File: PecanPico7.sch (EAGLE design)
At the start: 178 parts, among them IC1 Si4060-B1B-FM, IC10 TPS62260DRVT, IC11 TPS62261DRVT, IC12 TPS63021, IC13 RF6886, IC14 TPS78227DDCR, IC16 PAC1720-1-AIA-TR, IC2 Si4060-B1B-FM, IC3 BME280_BME280, IC4 uBlox MAX7/8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

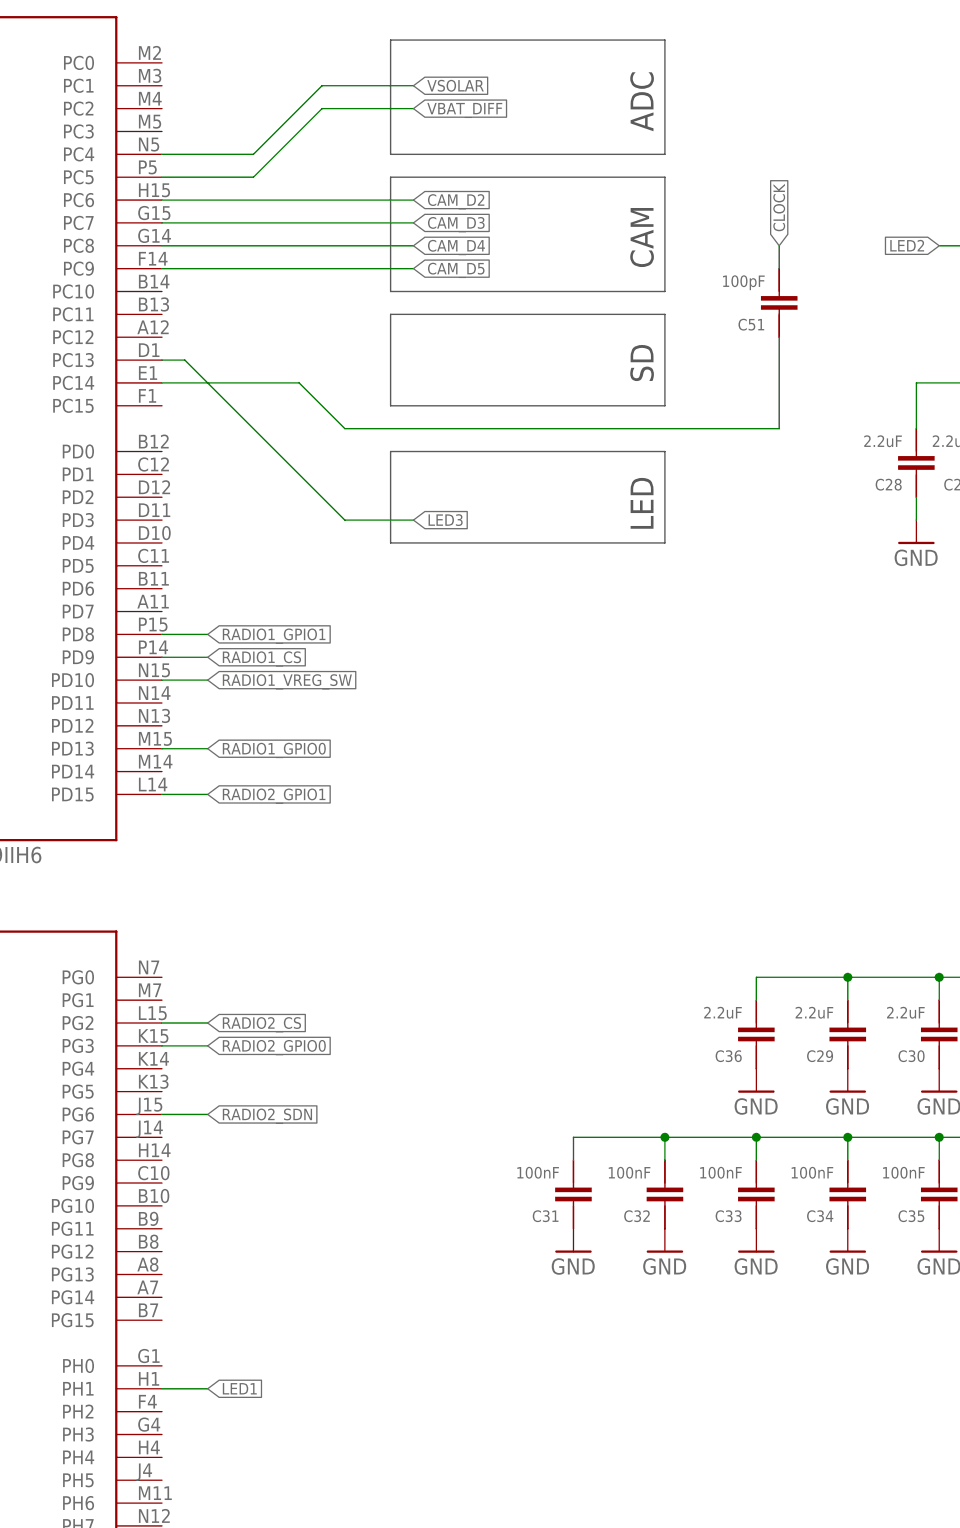
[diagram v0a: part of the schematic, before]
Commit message: Connected TCXO to STM32_OSC pin
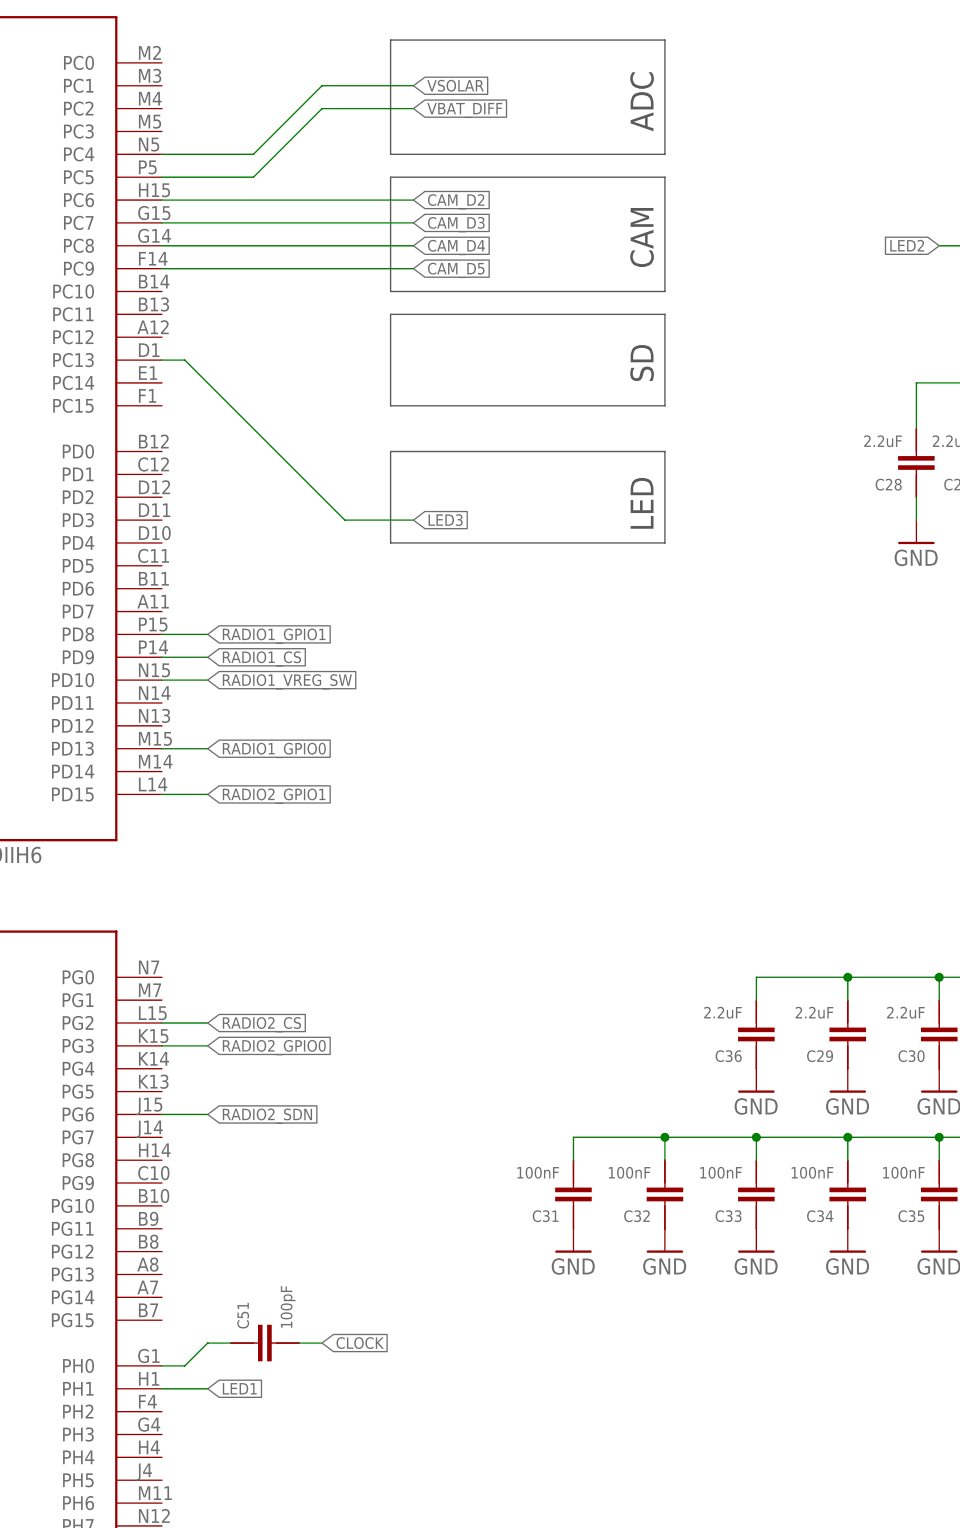
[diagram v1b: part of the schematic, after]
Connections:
- net N$39: now also IC5G$2.PH0; no longer IC5G$1.PC14
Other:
- moved on the sheet: C51
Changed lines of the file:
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@@
 <instance part="L14" gate="G$1" x="-22.86" y="447.04" rot="R180"/>
 <instance part="P+17" gate="G$1" x="10.16" y="447.04" rot="R270"/>
-<instance part="C51" gate="G$1" x="-76.2" y="195.58" rot="R180"/>
+<instance part="C51" gate="G$1" x="-134.62" y="81.28" rot="R90"/>
 <instance part="IC16" gate="A" x="-180.34" y="462.28"/>
 <instance part="P+23" gate="G$1" x="-200.66" y="482.6"/>
@@
 <segment>
 <pinref part="C51" gate="G$1" pin="1"/>
-<wire x1="-76.2" y1="200.66" x2="-76.2" y2="203.2" width="0.1524" layer="91"/>
-<label x="-76.2" y="203.2" size="1.27" layer="95" rot="R90" xref="yes"/>
+<wire x1="-129.54" y1="81.28" x2="-127" y2="81.28" width="0.1524" layer="91"/>
+<label x="-127" y="81.28" size="1.27" layer="95" xref="yes"/>
 </segment>
 <segment>
@@
 <net name="N$39" class="0">
 <segment>
-<pinref part="IC5" gate="G$1" pin="PC14"/>
-<wire x1="-144.78" y1="187.96" x2="-129.54" y2="187.96" width="0.1524" layer="91"/>
-<wire x1="-129.54" y1="187.96" x2="-124.46" y2="182.88" width="0.1524" layer="91"/>
-<wire x1="-124.46" y1="182.88" x2="-76.2" y2="182.88" width="0.1524" layer="91"/>
-<wire x1="-76.2" y1="182.88" x2="-76.2" y2="193.04" width="0.1524" layer="91"/>
 <pinref part="C51" gate="G$1" pin="2"/>
-</segment>
-</net>
+<wire x1="-137.16" y1="81.28" x2="-139.7" y2="81.28" width="0.1524" layer="91"/>
+<wire x1="-139.7" y1="81.28" x2="-142.24" y2="78.74" width="0.1524" layer="91"/>
+<wire x1="-142.24" y1="78.74" x2="-144.78" y2="78.74" width="0.1524" layer="91"/>
+<pinref part="IC5" gate="G$2" pin="PH0"/>
+</segment>
+</net>

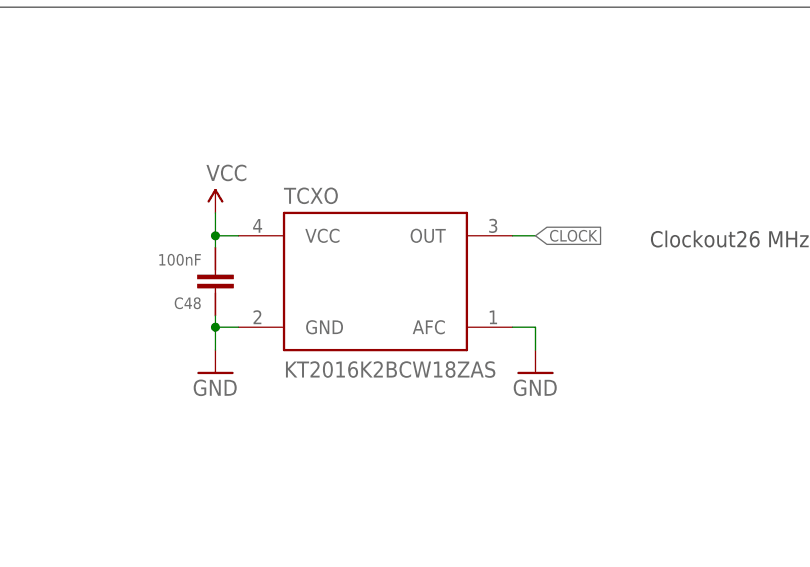
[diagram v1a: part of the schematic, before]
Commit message: Replaced small TCXO package to larger one
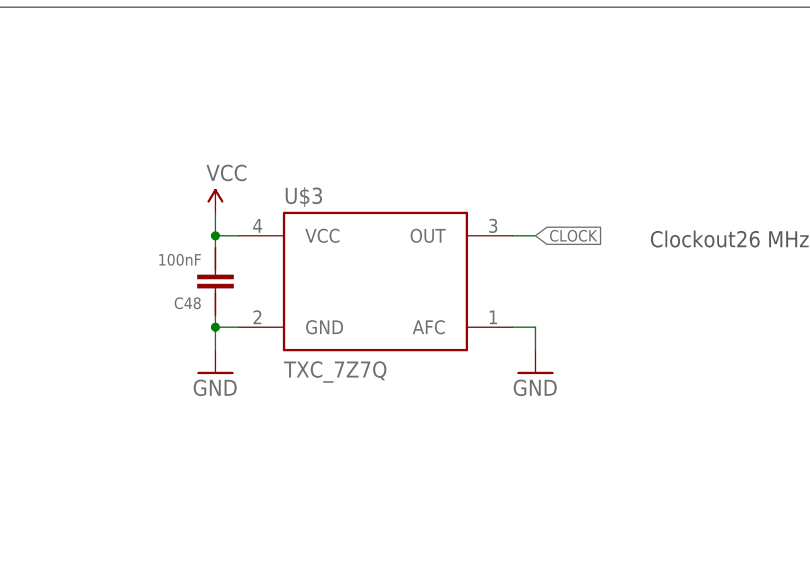
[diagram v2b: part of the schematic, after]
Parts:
- removed TCXO: KT2016K2BCW18ZAS, PecanFemto3:TXC_7Z
- added U$3: TXC_7Z7Q, PecanFemto3:TXC_7Z7Q
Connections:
- net CLOCK: now also U$3.OUT; no longer TCXO.OUT
- net GND: now also U$3.AFC, U$3.GND; no longer TCXO.AFC, TCXO.GND
- net VCC: now also U$3.VCC; no longer TCXO.VCC
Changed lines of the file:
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@@
 <?xml version="1.0" encoding="utf-8"?>
 <!DOCTYPE eagle SYSTEM "eagle.dtd">
-<eagle version="7.3.0">
+<eagle version="7.2.0">
 <drawing>
 <settings>
@@
 <part name="C47" library="PecanFemto3" deviceset="CAP-0805" device="" value="10uF"/>
 <part name="GND61" library="PecanPico6" deviceset="GND" device=""/>
-<part name="TCXO" library="PecanFemto3" deviceset="TXC_7Z" device="" value="KT2016K2BCW18ZAS"/>
 <part name="GND62" library="PecanPico6" deviceset="GND" device=""/>
 <part name="P+21" library="PecanPico6" deviceset="3.3V" device="" value="VCC"/>
@@
 <part name="GND122" library="PecanPico6" deviceset="GND" device=""/>
 <part name="GND123" library="PecanPico6" deviceset="GND" device=""/>
+<part name="U$3" library="PecanFemto3" deviceset="TXC_7Z" device="7Q"/>
 </parts>
 <sheets>
@@
 <instance part="C47" gate="G$1" x="-147.32" y="391.16"/>
 <instance part="GND61" gate="1" x="-147.32" y="373.38"/>
-<instance part="TCXO" gate="TCXO" x="175.26" y="60.96"/>
 <instance part="GND62" gate="1" x="157.48" y="50.8"/>
 <instance part="P+21" gate="G$1" x="157.48" y="68.58"/>
@@
 <instance part="GND122" gate="1" x="-17.78" y="469.9"/>
 <instance part="GND123" gate="1" x="-66.04" y="469.9"/>
+<instance part="U$3" gate="TCXO" x="175.26" y="60.96"/>
 </instances>
 <busses>
@@
 <pinref part="GND62" gate="1" pin="GND"/>
 <wire x1="157.48" y1="53.34" x2="157.48" y2="55.88" width="0.1524" layer="91"/>
-<pinref part="TCXO" gate="TCXO" pin="GND"/>
 <wire x1="157.48" y1="55.88" x2="160.02" y2="55.88" width="0.1524" layer="91"/>
 <pinref part="C48" gate="G$1" pin="2"/>
 <wire x1="157.48" y1="55.88" x2="157.48" y2="57.15" width="0.1524" layer="91"/>
 <junction x="157.48" y="55.88"/>
-</segment>
-<segment>
-<pinref part="TCXO" gate="TCXO" pin="AFC"/>
+<pinref part="U$3" gate="TCXO" pin="GND"/>
+</segment>
+<segment>
 <wire x1="190.5" y1="55.88" x2="193.04" y2="55.88" width="0.1524" layer="91"/>
 <wire x1="193.04" y1="55.88" x2="193.04" y2="53.34" width="0.1524" layer="91"/>
 <pinref part="GND63" gate="1" pin="GND"/>
+<pinref part="U$3" gate="TCXO" pin="AFC"/>
 </segment>
 <segment>
@@
 </segment>
 <segment>
-<pinref part="TCXO" gate="TCXO" pin="OUT"/>
 <wire x1="190.5" y1="66.04" x2="193.04" y2="66.04" width="0.1524" layer="91"/>
 <label x="193.04" y="66.04" size="1.27" layer="95" xref="yes"/>
+<pinref part="U$3" gate="TCXO" pin="OUT"/>
 </segment>
 <segment>
@@
 <pinref part="P+21" gate="G$1" pin="VCC"/>
 <wire x1="157.48" y1="66.04" x2="157.48" y2="68.58" width="0.1524" layer="91"/>
-<pinref part="TCXO" gate="TCXO" pin="VCC"/>
 <wire x1="160.02" y1="66.04" x2="157.48" y2="66.04" width="0.1524" layer="91"/>
 <pinref part="C48" gate="G$1" pin="1"/>
 <wire x1="157.48" y1="64.77" x2="157.48" y2="66.04" width="0.1524" layer="91"/>
 <junction x="157.48" y="66.04"/>
-</segment>
-<segment>
+<pinref part="U$3" gate="TCXO" pin="VCC"/>
+</segment>
+<segment>
